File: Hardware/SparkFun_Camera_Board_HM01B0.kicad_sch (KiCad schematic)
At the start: 50 parts, among them J1 Conn_01x09, J2 Conn_01x09, J3 Conn_01x09, J4 HM01B0, Q1 RE1C002UNTCL, Q2 RE1C002UNTCL, Q3 RE1C002UNTCL, Q4 RE1C002UNTCL, U1 HM01B0, U2 MIC5205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

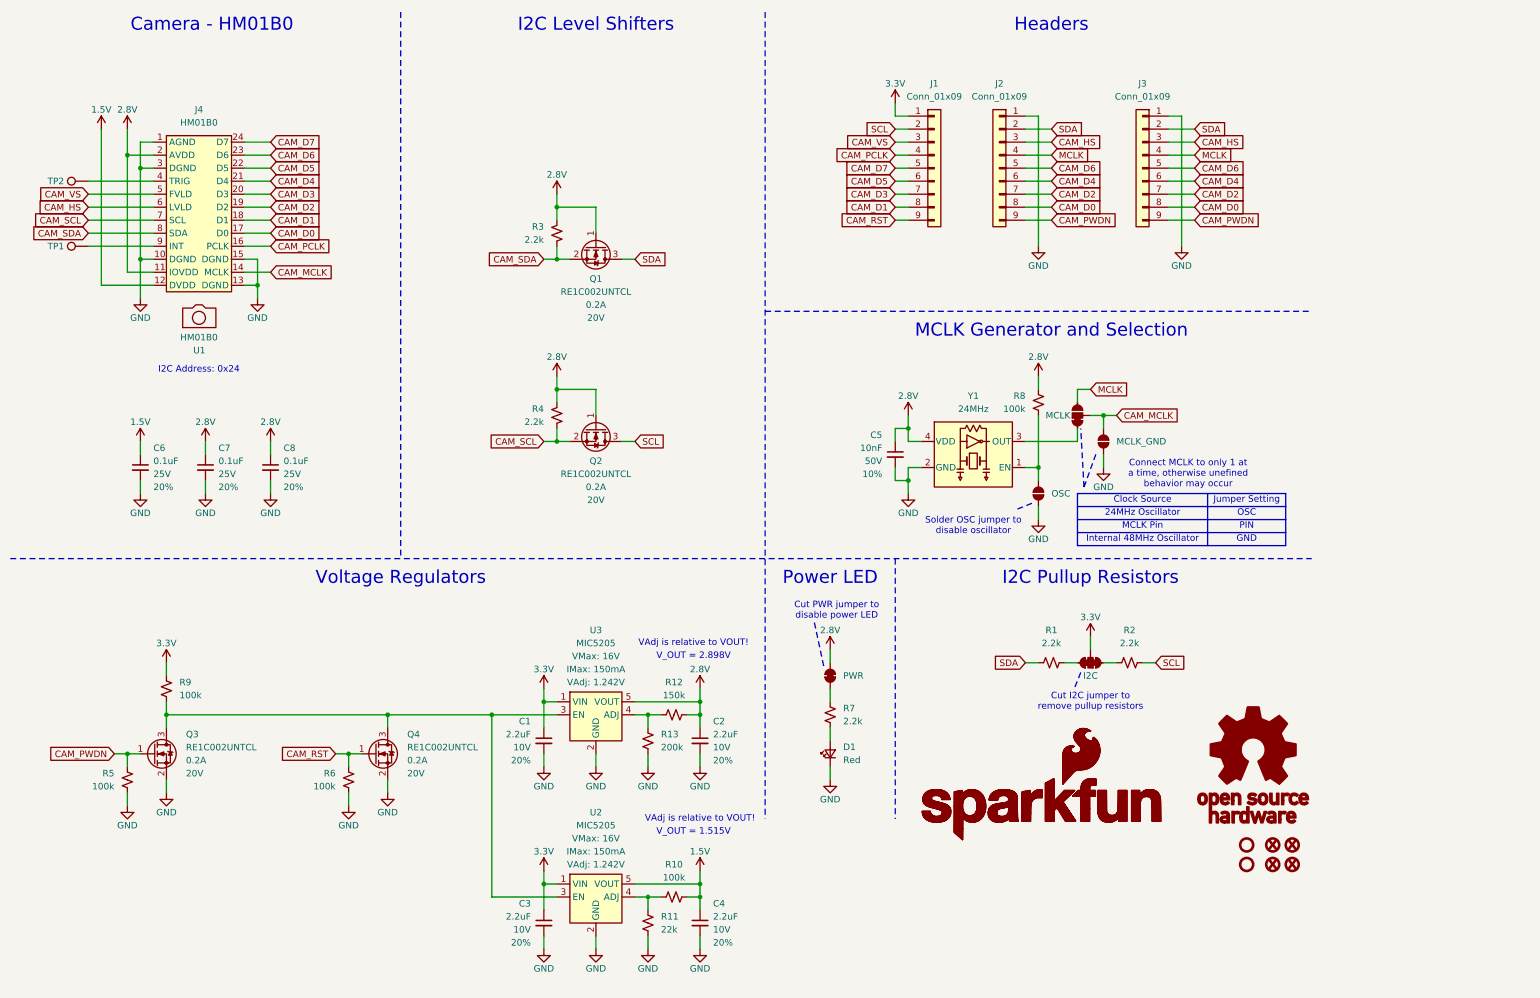
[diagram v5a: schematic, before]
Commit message: Update voltage regulaotrs
Remove 1.5V regulator (HM01B0 has internal 1.5V LDO)
Change 2.8V regulator to RT9080 (much lower quiescent current and ripple than MIC5205)
Add test points for 1.5V and 2.8V rails
Adjust power LED position
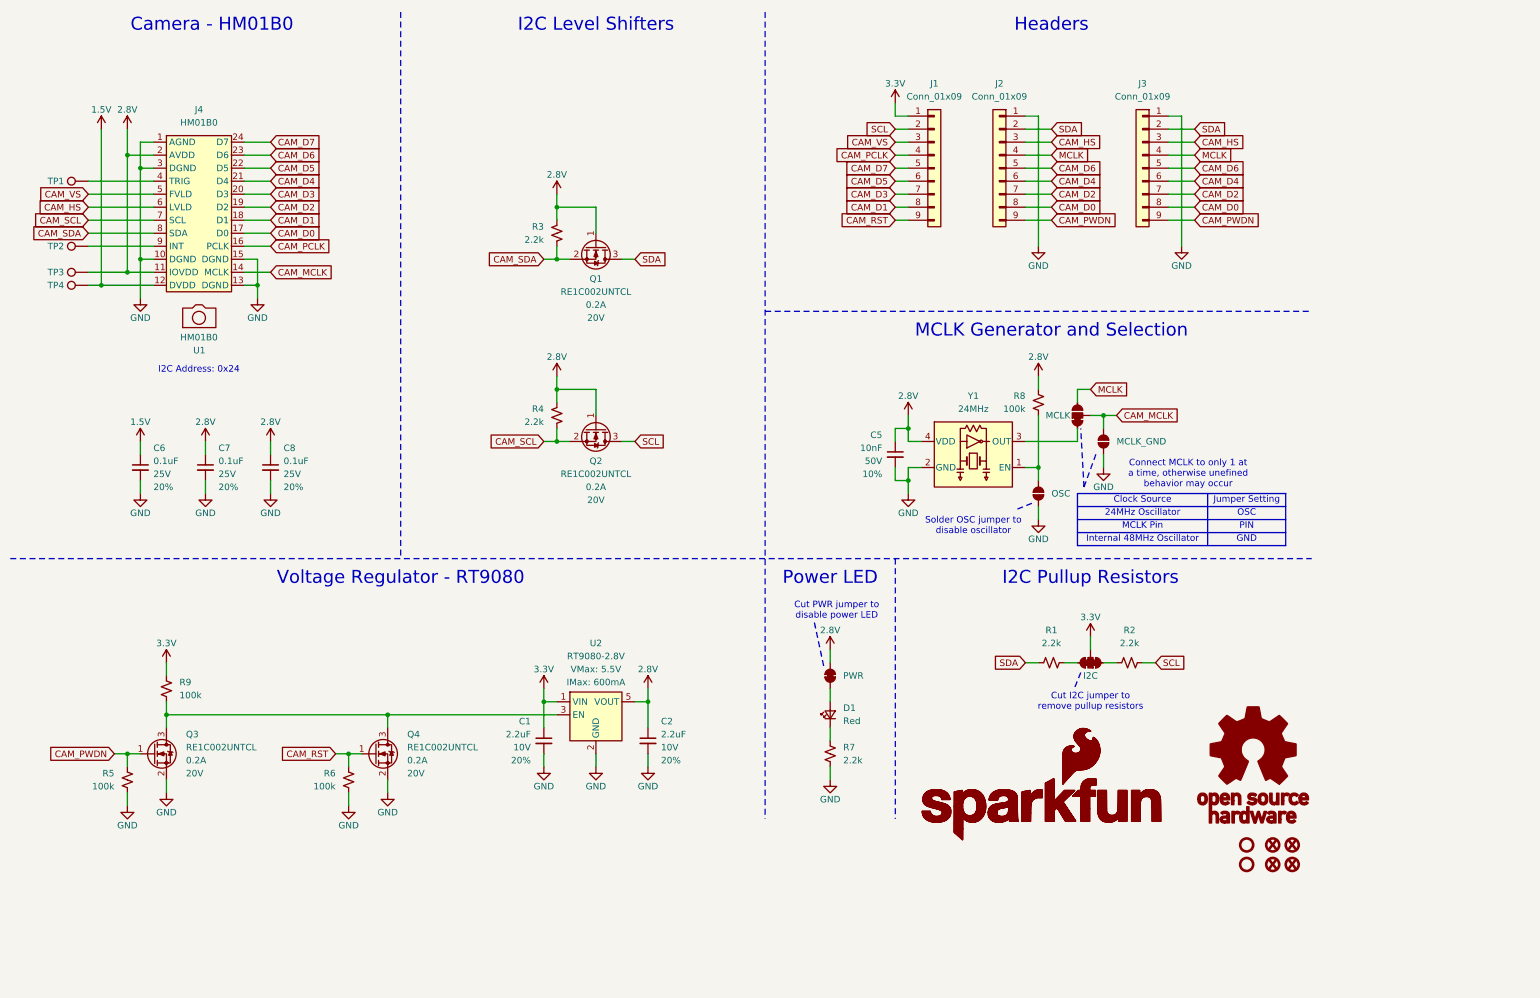
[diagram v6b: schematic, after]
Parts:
- removed C3, C4: 2.2uF, SparkFun-Capacitor:C_0603_1608Metric, symbol SparkFun-Capacitor:2.2uF_0603_10V_20%
- removed R10: 100k, SparkFun-Resistor:R_0603_1608Metric, symbol SparkFun-Resistor:100k_0603
- removed R11: 22k, SparkFun-Resistor:R_0603_1608Metric, symbol SparkFun-Resistor:22k_0603
- removed R12: 150k, SparkFun-Resistor:R_0603_1608Metric, symbol SparkFun-Resistor:150k_0603
- removed R13: 200k, SparkFun-Resistor:R_0603_1608Metric, symbol SparkFun-Resistor:200k_0603
- removed U2, U3: MIC5205, SparkFun-Semiconductor-Standard:SOT23-5, symbol SparkFun-Regulator:MIC5205
- added TP3, TP4: 1.25mm, SparkFun-Connector:TestPoint-1.25mm, symbol SparkFun-Connector:TestPoint_1.25mm
- added U2: RT9080-2.8V, SparkFun-Semiconductor-Standard:SOT23-5, symbol SparkFun-Regulator:RT9080-2.8
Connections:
- net 1.5V: now also TP4.1
- net 2.8V: now also TP3.1, U2.5 (VOUT)
- net 3.3V: now also U2.1 (VIN)
- net GND: now also R7.1, U2.2 (GND); no longer D1.1 (K)
- net at Q3.3 (D), Q4.3 (D), R9.2: now also U2.3 (EN)
- net at TP1.1: now also J4.4 (TRIG); no longer J4.9 (INT)
- net at D1.2 (A): now also JP7.1 (A); no longer R7.1
- net at R7.2: now also D1.1 (K); no longer JP7.1 (A)
- net at TP2.1: now also J4.9 (INT); no longer J4.4 (TRIG)
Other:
- note added: "Voltage Regulator - RT9080"
- note removed: "VAdj is relative to VOUT!"
- note removed: "V_OUT = 1.515V"
- note removed: "V_OUT = 2.898V"
- note removed: "Voltage Regulators"
- moved on the sheet: C2, D1, R7, TP1, TP2

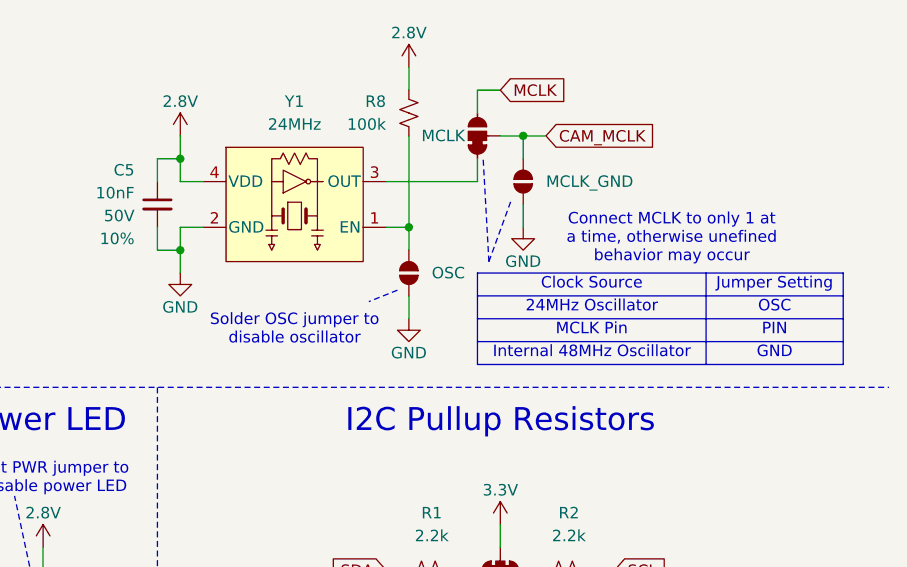
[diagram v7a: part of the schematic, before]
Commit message: Design review updates
Rename OSC jumper to OSC_DIS
Add default text to MCLK jumper table
Clarify MCLK PTH Pad in MCLK jumper table
Fix typo in MCLK jumper table
Fix LED datasheet
Change MCLK pad silk labels to non-inverted
Add GND via to fix GND peninsula on side of board
Remove GND vias creating islands between data pins
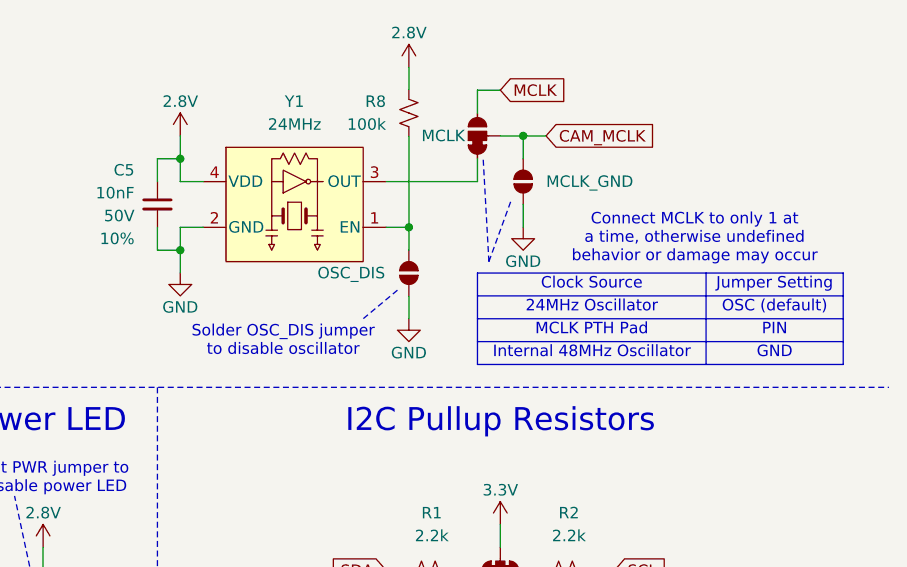
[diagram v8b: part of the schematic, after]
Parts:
- JP5: value OSC -> OSC_DIS
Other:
- note added: "Connect MCLK to only 1 at a time, otherwise undefined behavior or damage may occur"
- note added: "MCLK PTH Pad"
- note added: "OSC (default)"
- note added: "Solder OSC_DIS jumper to disable oscillator"
- note removed: "Connect MCLK to only 1 at a time, otherwise unefined behavior may occur"
- note removed: "MCLK Pin"
- note removed: "OSC"
- note removed: "Solder OSC jumper to disable oscillator"
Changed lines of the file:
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@@
 	(polyline
 		(pts
-			(xy 212.09 108.585) (xy 208.915 109.855)
+			(xy 212.09 108.585) (xy 208.28 111.76)
 		)
 		(stroke
@@
 		)
 	)
-	(text "Connect MCLK to only 1 at\na time, otherwise unefined\nbehavior may occur"
+	(text "Connect MCLK to only 1 at\na time, otherwise undefined\nbehavior or damage may occur"
 		(exclude_from_sim no)
-		(at 242.57 102.87 0)
+		(at 245.11 102.87 0)
 		(effects
 			(font
@@
 		)
 	)
-	(text "Solder OSC jumper to\ndisable oscillator"
+	(text "Solder OSC_DIS jumper\nto disable oscillator"
 		(exclude_from_sim no)
-		(at 200.66 113.03 0)
+		(at 199.39 114.3 0)
 		(effects
 			(font
@@
 		)
 	)
-	(text "OSC"
+	(text "OSC (default)"
 		(exclude_from_sim no)
 		(at 254 110.49 0)
@@
 		)
 	)
-	(text "MCLK Pin"
+	(text "MCLK PTH Pad"
 		(exclude_from_sim no)
 		(at 233.68 113.03 0)
@@
 			)
 		)
-		(property "Datasheet" "https://docs.broadcom.com/docs/AV02-0551EN"
+		(property "Datasheet" "https://www.kingbrightusa.com/images/catalog/SPEC/APT1608SURCK.pdf"
 			(at 182.88 149.86 0)
 			(effects
@@
 		(on_board yes)
 		(dnp no)
-		(fields_autoplaced yes)
 		(property "Reference" "JP5"
 			(at 208.28 106.68 90)
@@
 			)
 		)
-		(property "Value" "OSC"
-			(at 215.9 106.6799 90)
+		(property "Value" "OSC_DIS"
+			(at 203.2 106.68 90)
 			(effects
 				(font
